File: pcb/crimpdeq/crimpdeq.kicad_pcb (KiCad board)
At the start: 2 copper layers, 23 x 63.8 mm, 53 parts, among them J2 USB4105-GF-A, Q1 SS8550, Q2 DMG3415U, SW1 SW_Push, SW2 SW_Push, U1 ESP32-C3-MINI-1, U2 MCP73831T-2ACI/OT, U3 HX711, U4 Rust_Board, U6 SY8088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

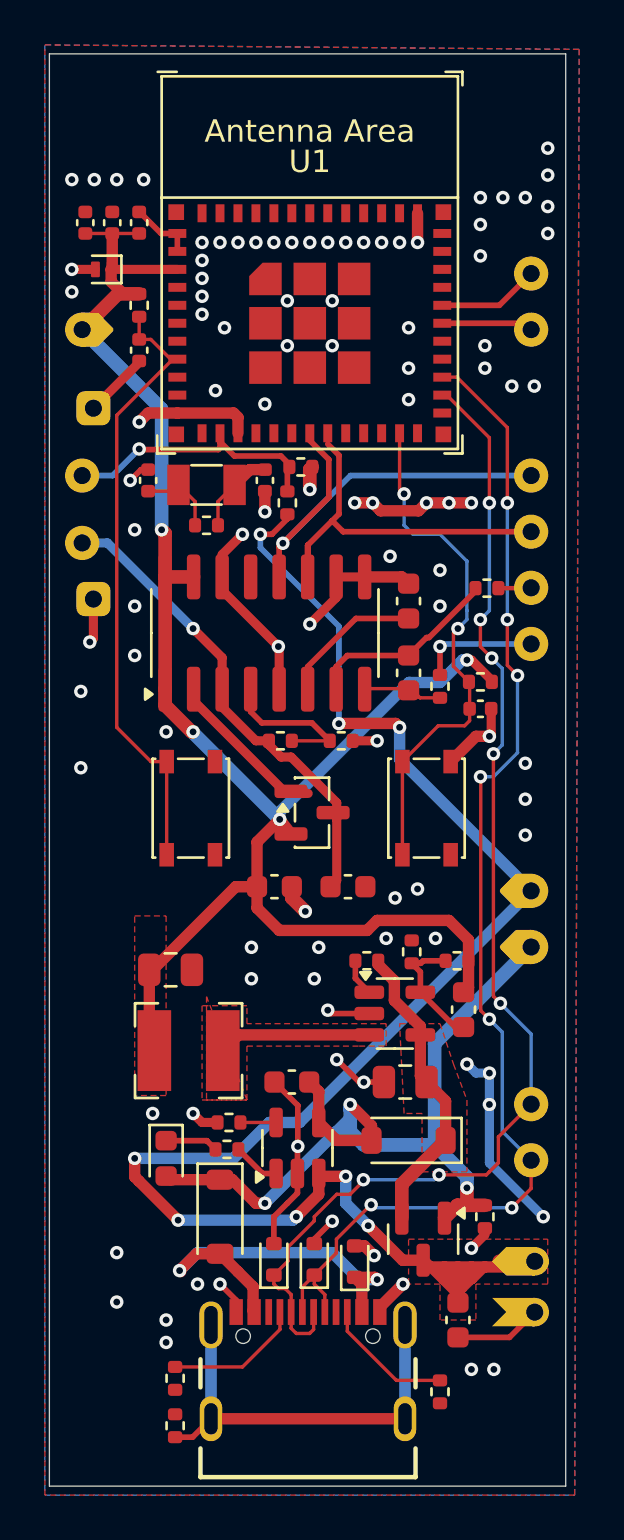
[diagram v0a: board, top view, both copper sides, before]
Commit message: fix: trim U4 pads and reroute board
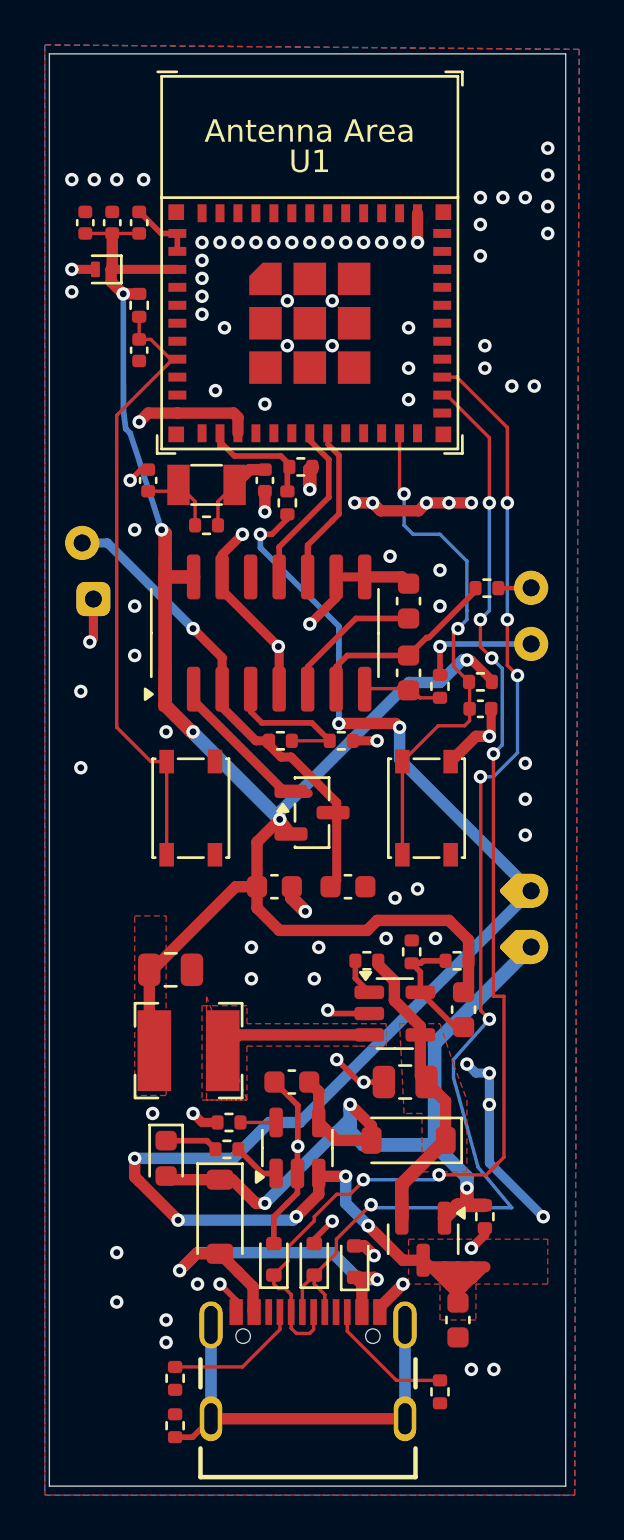
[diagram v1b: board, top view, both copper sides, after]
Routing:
- net IO4_DATA: track 20.4 -> 8.08 mm, vias 1 -> 0
- net IO5_SCK: track 17.2 -> 8.11 mm
- net GND: track 78.1 -> 71.3 mm
- net IO1_ADC: track 12.4 -> 5.78 mm, vias 1 -> 0
- net IO21_TX: track 4.55 -> 0.00 mm
- net IO20_RX: track 4.08 -> 0.00 mm
- net +BATT: track 80.8 -> 76.9 mm
- net +3V3: track 80.1 -> 77.3 mm, vias 4 -> 5
- net USB_D-: track 54.6 -> 53.9 mm, vias 7 -> 6
- net USB_D+: track 55.8 -> 55.5 mm, vias 7 -> 6

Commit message: fix: remove unused rtc crystal option
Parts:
- removed C7, C8: DNP, Capacitor_SMD:C_0402_1005Metric
- removed R4: DNP, Resistor_SMD:R_0402_1005Metric
- removed Y1: 32.768Hz, Crystal:Crystal_SMD_3215-2Pin_3.2x1.5mm
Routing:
- net IO1: track 4.13 -> 0.00 mm
- net IO0: track 3.57 -> 0.00 mm

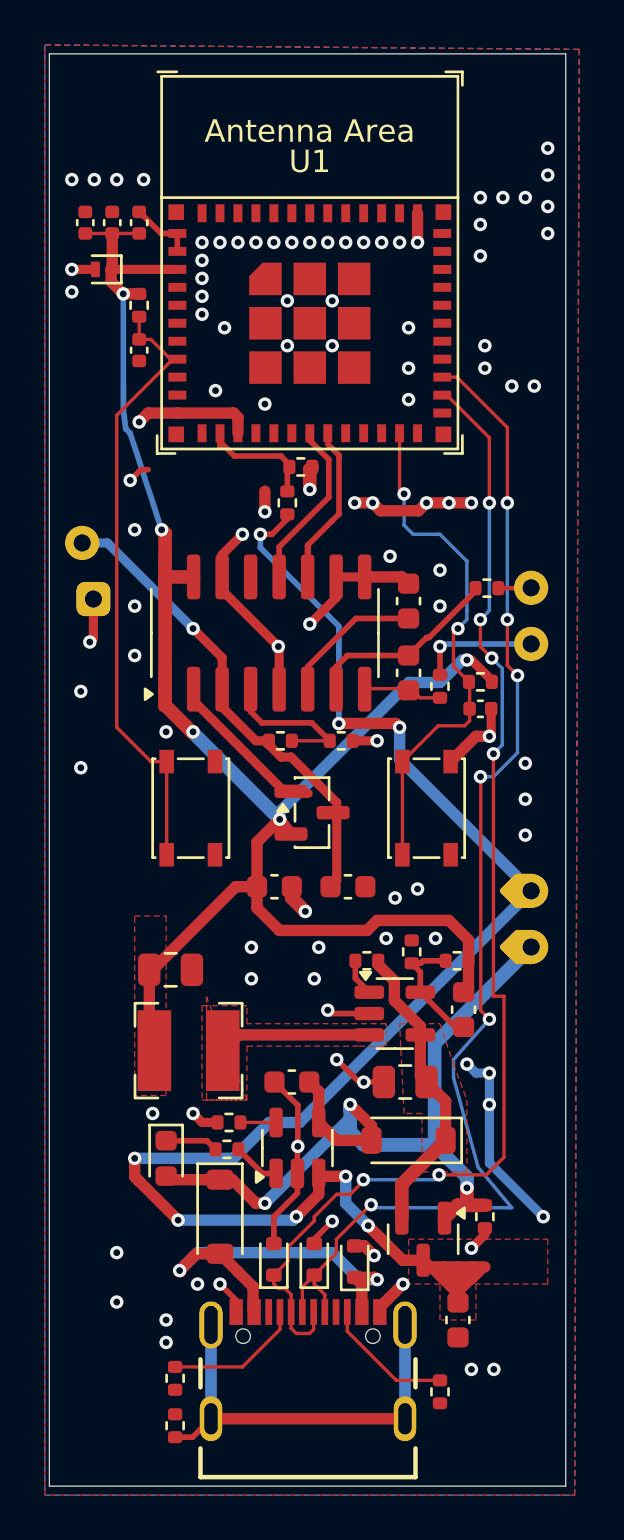
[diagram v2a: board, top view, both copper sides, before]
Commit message: fix: allow battery charging while powered off
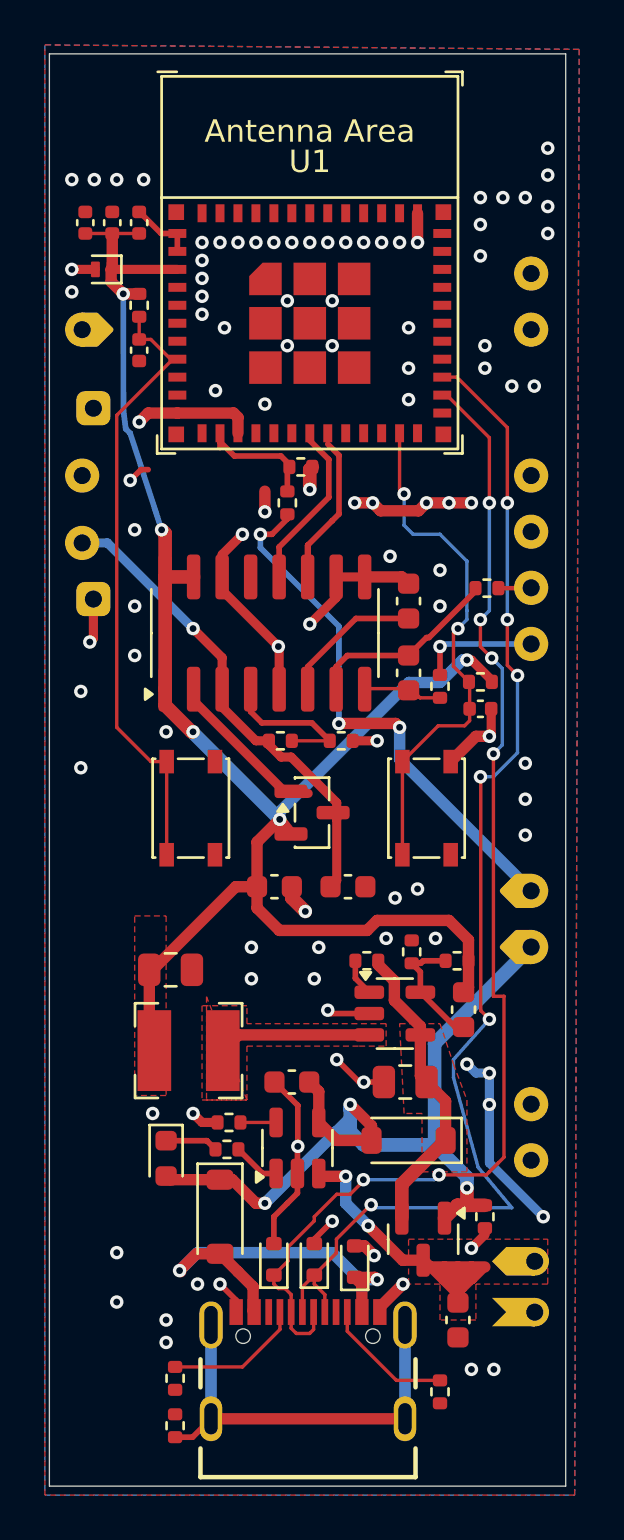
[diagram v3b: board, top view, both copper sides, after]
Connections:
- R12 pad 1: +BATT -> VBAT_SW
- U4 pad 11: +BATT -> VBAT_SW
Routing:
- net +BATT: track 76.9 -> 19.0 mm, vias 8 -> 2
- net 59: track 0.00 -> 24.1 mm, vias 0 -> 3

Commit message: refactor: clarify system power rail naming
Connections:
- net +5V renamed VSYS
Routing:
- net VSYS: track 13.5 -> 0.00 mm
- net +5V: track 0.00 -> 13.5 mm
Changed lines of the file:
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@@
 		(sheetfile "crimpdeq.kicad_sch")
 		(attr smd)
-		(duplicate_pad_numbers_are_jumpers no)
 		(fp_line
 			(start 0 -1.56)
@@
 			(layers "F.Cu" "F.Mask" "F.Paste")
 			(roundrect_rratio 0.25)
-			(net "+5V")
+			(net "VSYS")
 			(pinfunction "IN")
 			(pintype "power_in")
@@
 		(sheetfile "crimpdeq.kicad_sch")
 		(attr smd)
-		(duplicate_pad_numbers_are_jumpers no)
 		(fp_line
 			(start 0 1.56)
@@
 			(layers "F.Cu" "F.Mask" "F.Paste")
 			(roundrect_rratio 0.25)
-			(net "+5V")
+			(net "VSYS")
 			(pinfunction "S")
 			(pintype "passive")
@@
 		(sheetfile "crimpdeq.kicad_sch")
 		(attr smd)
-		(duplicate_pad_numbers_are_jumpers no)
 		(fp_line
 			(start -2.36 1)
@@
 			(layers "F.Cu" "F.Mask" "F.Paste")
 			(roundrect_rratio 0.25)
-			(net "+5V")
+			(net "VSYS")
 			(pinfunction "K")
 			(pintype "passive")
@@
 		(sheetfile "crimpdeq.kicad_sch")
 		(attr smd)
-		(duplicate_pad_numbers_are_jumpers no)
 		(fp_line
 			(start -0.153641 0.38)
@@
 			(layers "F.Cu" "F.Mask" "F.Paste")
 			(roundrect_rratio 0.25)
-			(net "+5V")
+			(net "VSYS")
 			(pintype "passive")
 		)
@@
 		(sheetfile "crimpdeq.kicad_sch")
 		(attr smd)
-		(duplicate_pad_numbers_are_jumpers no)
 		(fp_line
 			(start -0.261252 0.735)
@@
 			(layers "F.Cu" "F.Mask" "F.Paste")
 			(roundrect_rratio 0.25)
-			(net "+5V")
+			(net "VSYS")
 			(pintype "passive")
 		)
@@
 	)
 	(zone
-		(net "+5V")
+		(net 13)
+		(net_name "VSYS")
 		(layer "F.Cu")
 		(hatch edge 0.5)
@@
 		)
 		(min_thickness 0.25)
+		(filled_areas_thickness no)
 		(fill yes
 			(thermal_gap 0.5)
 			(thermal_bridge_width 0.5)
-			(island_removal_mode 0)
 		)
 		(polygon
